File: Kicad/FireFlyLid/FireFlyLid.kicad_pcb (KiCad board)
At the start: 2 copper layers, 81.3 x 81.3 mm, 52 parts, among them J1 HEADER_4, J2 HEADER_1, J3 HEADER_1, SW1 SW_SPDT, U1 MSP430G2553IPW28, U2 MAXIM_MAX44009, X1 32K

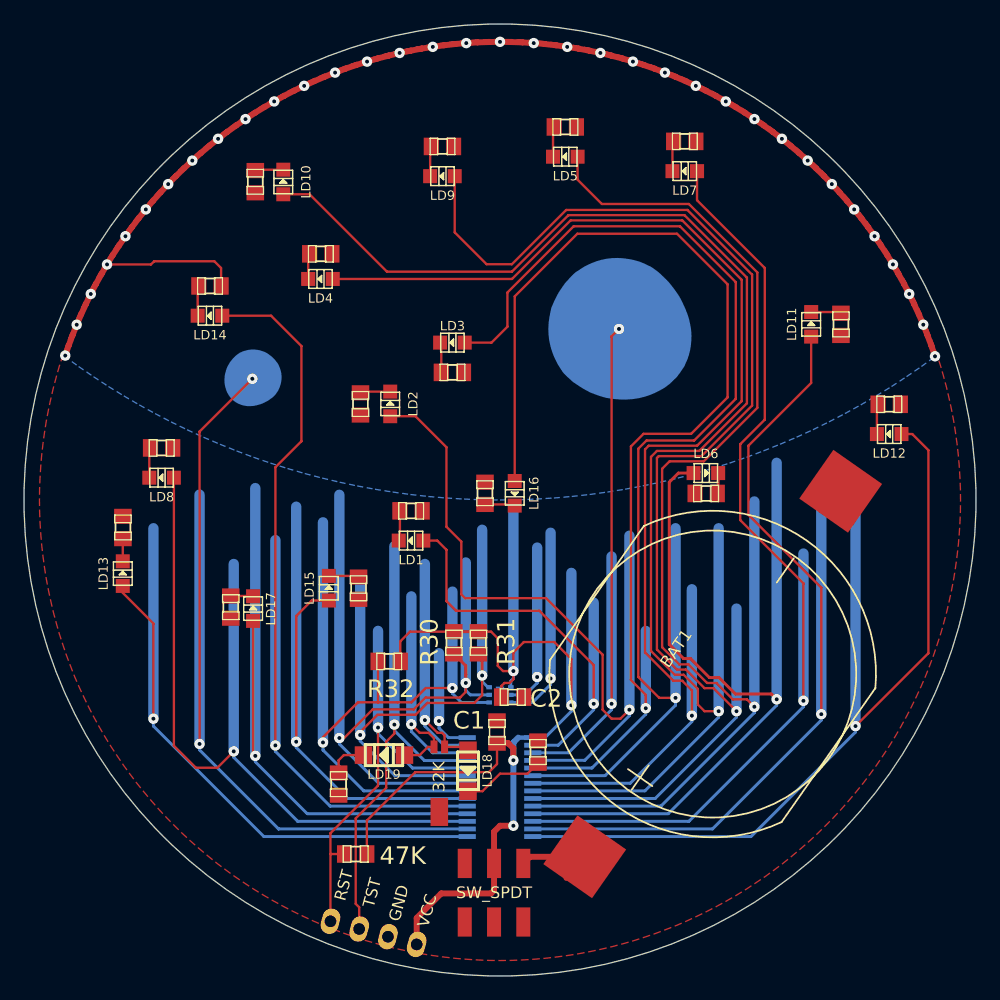
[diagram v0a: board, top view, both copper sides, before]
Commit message: New layout with off board battery and local vreg to 3.0 V
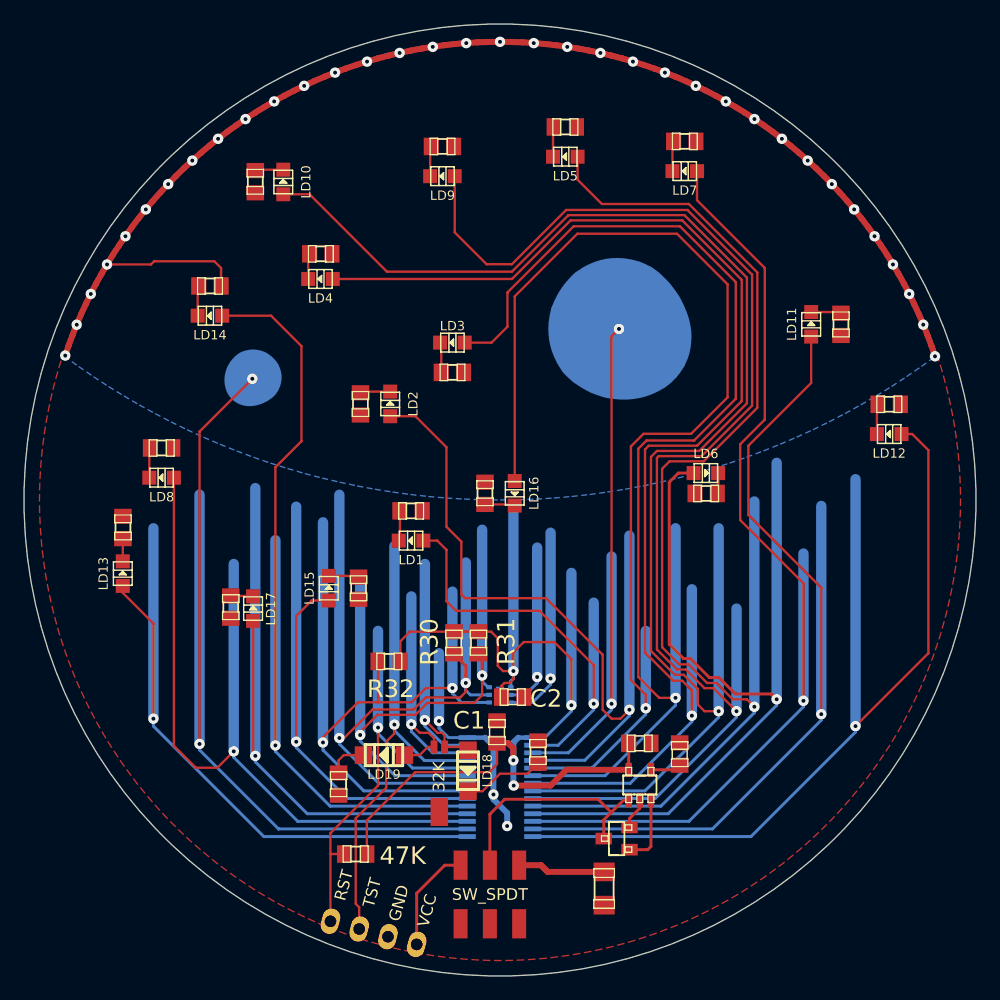
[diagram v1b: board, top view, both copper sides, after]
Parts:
- added C3: 1uF, dp_devices-C805, F.Cu at (220.2, 168.1)
- added C4: 470pF, dp_devices-C805, F.Cu at (223.6, 169.0)
- added VDET1: VDETECTOR_3PINS-SOT-223, dp_devices-SOT-23, F.Cu at (218.2, 176.2)
- added VREG1: VREG_5PINS-SOT-23-5, dp_devices-SOT-23-5, F.Cu at (220.2, 171.7)
- BAT1: footprint MPD_BU2450SM -> dp_devices-R1206
- moved BAT1 20.5 mm to (217.2, 180.5), turned to 270 degrees
- moved SW1 0.39 mm to (207.4, 181.0)
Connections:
- net GND renamed /GND
- J1 pad 1: /VCC -> /PROG_VCC
- SW1 pad 2: /VCC -> N-0000033
- SW1 pad 3: (no net) -> /PROG_VCC
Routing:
- net N-0000033: track 0.00 -> 20.1 mm
- net /GND: track 149.9 -> 162.4 mm, vias 38 -> 40
- net /PROG_VCC: track 0.00 -> 9.11 mm
- net /VCC: track 106.4 -> 98.9 mm
- net N-0000024: track 0.00 -> 5.89 mm
- net N-0000023: track 0.00 -> 2.62 mm
